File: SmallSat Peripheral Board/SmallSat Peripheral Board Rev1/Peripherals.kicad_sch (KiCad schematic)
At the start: 8 parts, among them U11 PPJA138K, U12 LMT88DCKR, U13 CSI-Connector

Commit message: ADCS Driver Work
Nothing final yet
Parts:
- removed U13: CSI-Connector, symbol SmallSat-Peripherals-Board:CSI-Connector
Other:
- sheet Sun Sensor Array1 ports: added 5V; removed 3V3

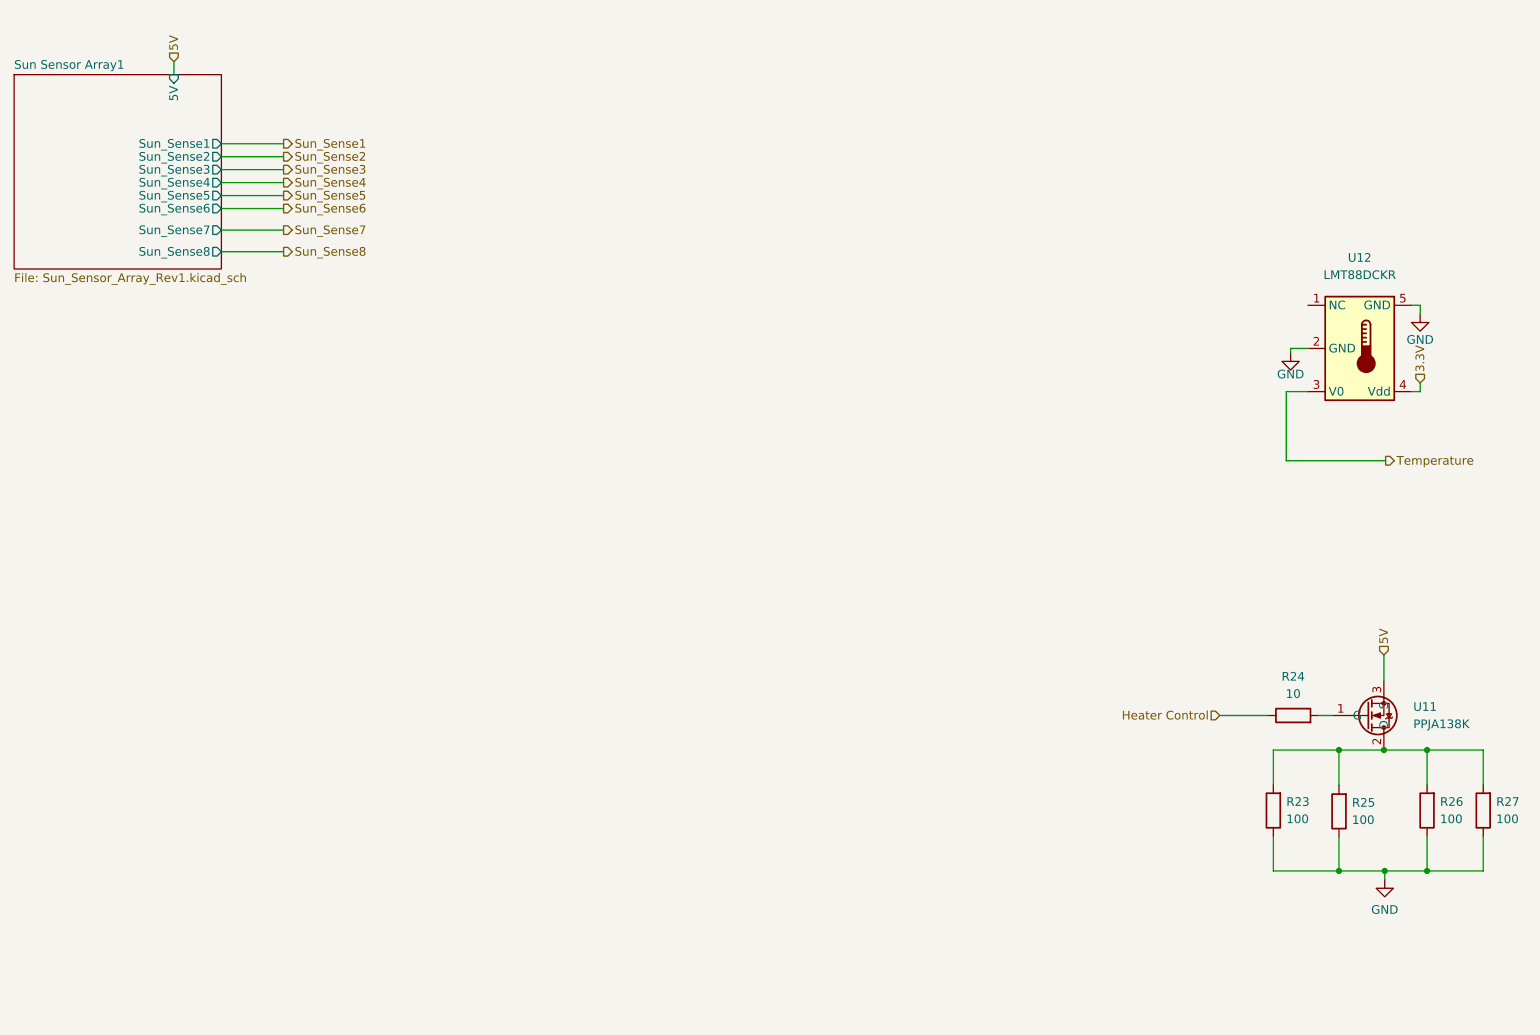
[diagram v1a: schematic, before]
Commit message: ADCS Driver Rev 2
- Redesigned the ESC with modern ICs that have bootstrapping infrastructure
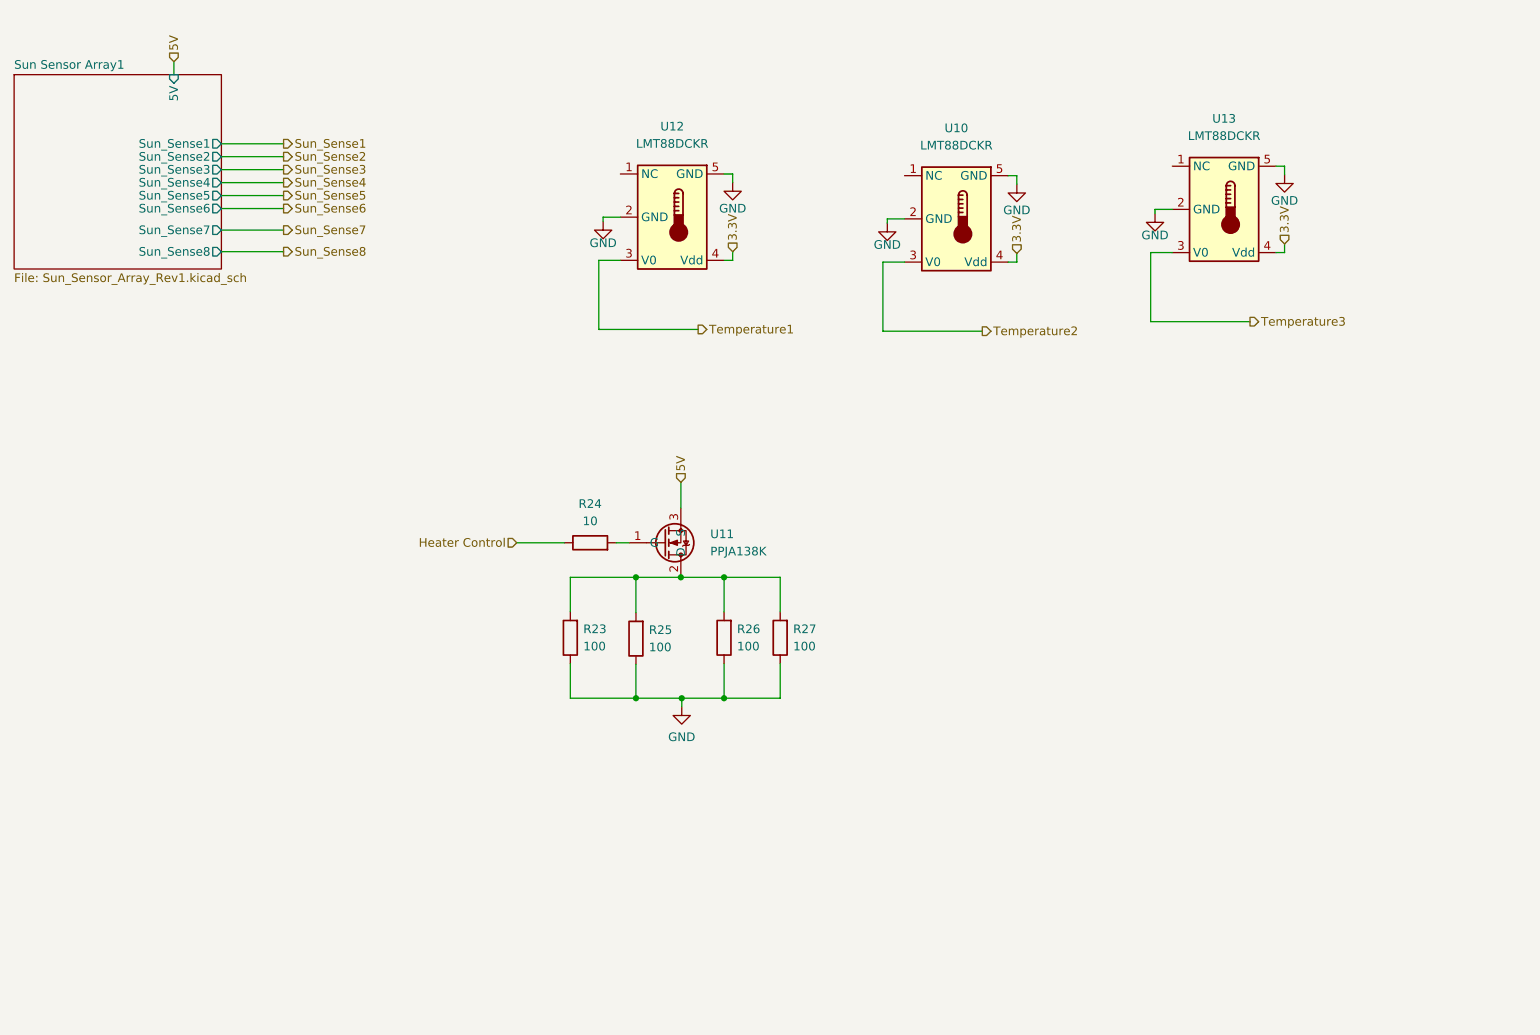
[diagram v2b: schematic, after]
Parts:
- added U10, U13: LMT88DCKR, symbol SmallSat-Peripherals-Board:LMT88DCKR
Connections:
- net 3.3V: now also U10.4 (Vdd), U13.4 (Vdd)
- net GND: now also U10.2 (GND), U10.5 (GND), U13.2 (GND), U13.5 (GND)
- net Temperature renamed Temperature1
- new net Temperature2: U10.3 (V0)
- new net Temperature3: U13.3 (V0)
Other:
- moved on the sheet: R23, R24, R25, R26, R27, U11, U12
